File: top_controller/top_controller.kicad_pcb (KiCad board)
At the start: 2 copper layers, 207.4 x 54.2 mm, 117 parts, among them J1 OUT1, J10 USB_C_Receptacle_USB2.0, J11 SWD, J12 UART, J13 BOOT0, J14 BOOT1, J2 OUT2, J3 OUT3, J4 OUT4, J5 OUT5, J6 OUT6, J7 OUT7, J8 OUT8, J9 PIN, SW1 RESET, U1 STM32F103C8Tx, U2 LT3045xMSE, U3 AD5754BREZ, U4 AD5754BREZ, U5 REF192, U6 EPM78V2, U7 REF192, Y1 8MHz

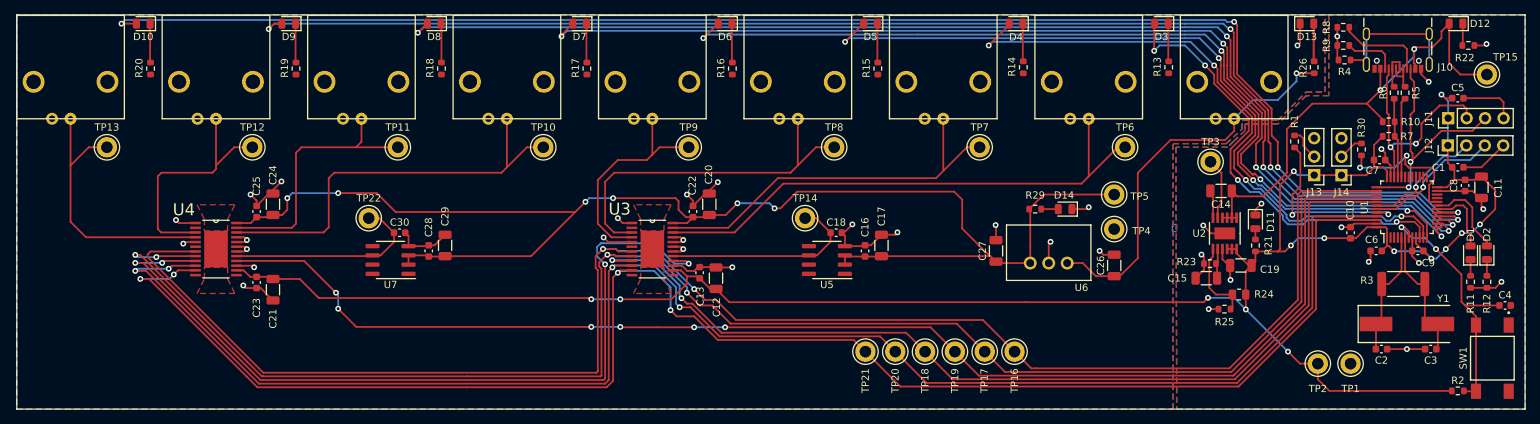
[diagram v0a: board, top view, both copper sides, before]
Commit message: DRC errors solved
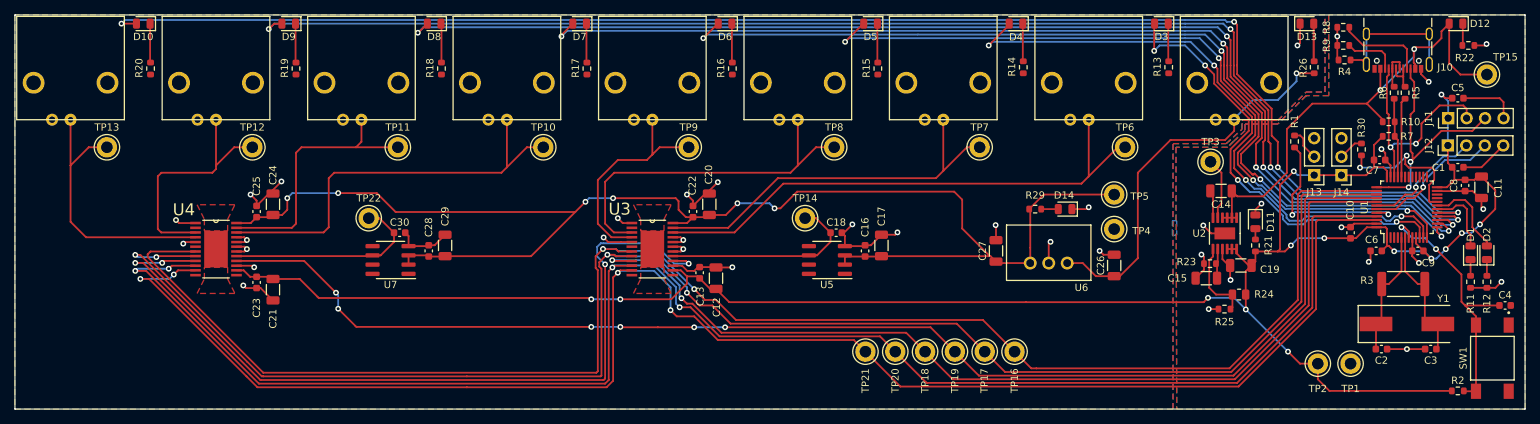
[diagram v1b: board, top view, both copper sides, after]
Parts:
- moved J1 0.13 mm to (180.0, 40.1)
- moved J2 0.13 mm to (160.0, 40.1)
- moved J3 0.13 mm to (140.0, 40.1)
- moved J4 0.13 mm to (120.0, 40.1)
- moved J5 0.13 mm to (100.0, 40.1)
- moved J6 0.13 mm to (80.0, 40.1)
- moved J7 0.13 mm to (60.0, 40.1)
- moved J8 0.13 mm to (40.0, 40.1)
- moved J9 0.13 mm to (200.0, 40.1)
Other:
- board size 207.4 x 54.2 mm -> 207.7 x 54.2 mm
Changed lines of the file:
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@@
   )
   (footprint "CONBNC002:CONBNC002" (layer "F.Cu")
-    (at 120 40)
+    (at 120 40.13)
     (property "Sheetfile" "top_controller.kicad_sch")
     (property "Sheetname" "")
@@
   )
   (footprint "CONBNC002:CONBNC002" (layer "F.Cu")
-    (at 200 40)
+    (at 200 40.13)
     (property "Sheetfile" "top_controller.kicad_sch")
     (property "Sheetname" "")
@@
   )
   (footprint "CONBNC002:CONBNC002" (layer "F.Cu")
-    (at 180 40)
+    (at 180 40.13)
     (property "Sheetfile" "top_controller.kicad_sch")
     (property "Sheetname" "")
@@
   )
   (footprint "CONBNC002:CONBNC002" (layer "F.Cu")
-    (at 60 40)
+    (at 60 40.13)
     (property "Sheetfile" "top_controller.kicad_sch")
     (property "Sheetname" "")
@@
   )
   (footprint "CONBNC002:CONBNC002" (layer "F.Cu")
-    (at 80 40)
+    (at 80 40.13)
     (property "Sheetfile" "top_controller.kicad_sch")
     (property "Sheetname" "")
@@
   )
   (footprint "CONBNC002:CONBNC002" (layer "F.Cu")
-    (at 100 40)
+    (at 100 40.13)
     (property "Sheetfile" "top_controller.kicad_sch")
     (property "Sheetname" "")
@@
   )
   (footprint "CONBNC002:CONBNC002" (layer "F.Cu")
-    (at 40 40)
+    (at 40 40.13)
     (property "Sheetfile" "top_controller.kicad_sch")
     (property "Sheetname" "")
@@
   )
   (footprint "CONBNC002:CONBNC002" (layer "F.Cu")
-    (at 160 40)
+    (at 160 40.13)
     (property "Sheetfile" "top_controller.kicad_sch")
     (property "Sheetname" "")
@@
   )
   (footprint "CONBNC002:CONBNC002" (layer "F.Cu")
-    (at 140 40)
+    (at 140 40.13)
     (property "Sheetfile" "top_controller.kicad_sch")
     (property "Sheetname" "")
@@
   (gr_line (start 240 85) (end 240 30.8)
     (stroke (width 0.1) (type default)) (layer "Edge.Cuts"))
-  (gr_line (start 32.6 30.8) (end 32.6 85)
+  (gr_line (start 32.35 30.8) (end 32.35 85)
     (stroke (width 0.1) (type default)) (layer "Edge.Cuts"))
-  (gr_line (start 32.6 85) (end 240 85)
+  (gr_line (start 32.35 85) (end 240 85)
     (stroke (width 0.1) (type default)) (layer "Edge.Cuts"))
-  (gr_line (start 240 30.8) (end 32.6 30.8)
+  (gr_line (start 240 30.8) (end 32.35 30.8)
     (stroke (width 0.1) (type default)) (layer "Edge.Cuts"))
   (segment (start 202.92 63.325) (end 206 63.325) (width 0.25) (layer "F.Cu") (net 1))
@@
         (xy 212.5 41.4)
         (xy 212.5 30.8)
-        (xy 32.6 30.8)
-        (xy 32.6 85)
+        (xy 32.35 30.8)
+        (xy 32.35 85)
       )
     )
@@
     (polygon
       (pts
-        (xy 191.5 59.6)
-        (xy 192.1 59.6)
-        (xy 192.1 60.6)
-        (xy 191.5 60.6)
+        (xy 191.5 59.1)
+        (xy 192.1 59.1)
+        (xy 192.1 61.1)
+        (xy 191.5 61.1)
       )
     )

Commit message: Made power traces wider
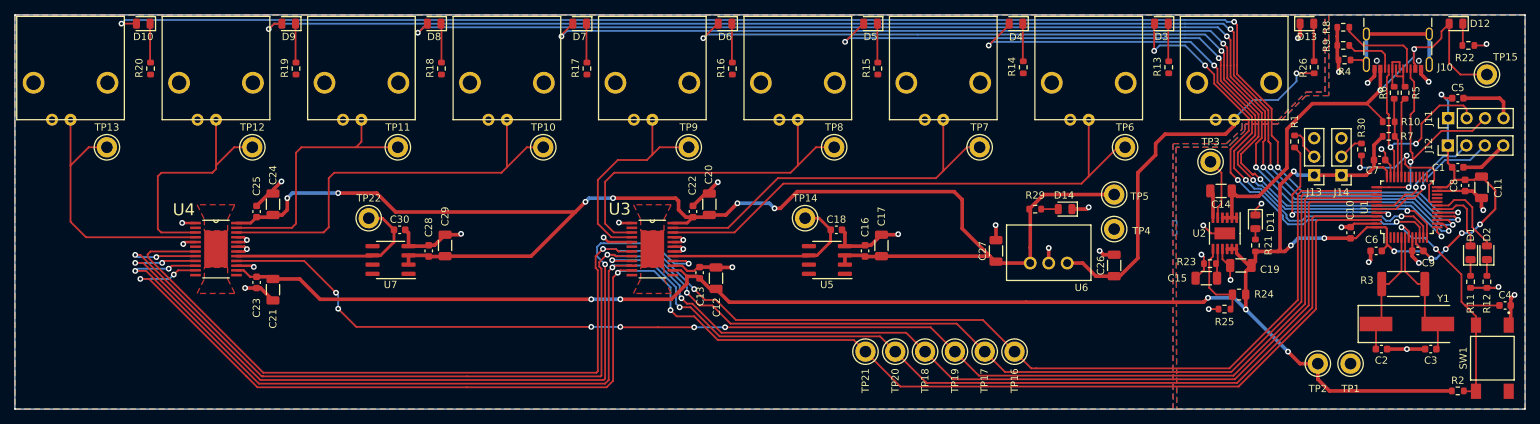
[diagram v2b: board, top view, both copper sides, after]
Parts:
- moved C18 0.40 mm to (145.3, 60.4)
- moved C30 0.40 mm to (85.2, 60.4)
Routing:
- net GND: track 161.5 -> 163.0 mm
- net +3V3: track 296.9 -> 297.9 mm
